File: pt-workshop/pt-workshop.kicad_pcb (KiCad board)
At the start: 2 copper layers, 53 parts, among them J101 Conn_01x10, J102 Conn_01x10, Q301 NST65011, Q401 J201, Q402 3904 BEC, U201 L78L05, U202 PT2399-Detailed, U301 TL972

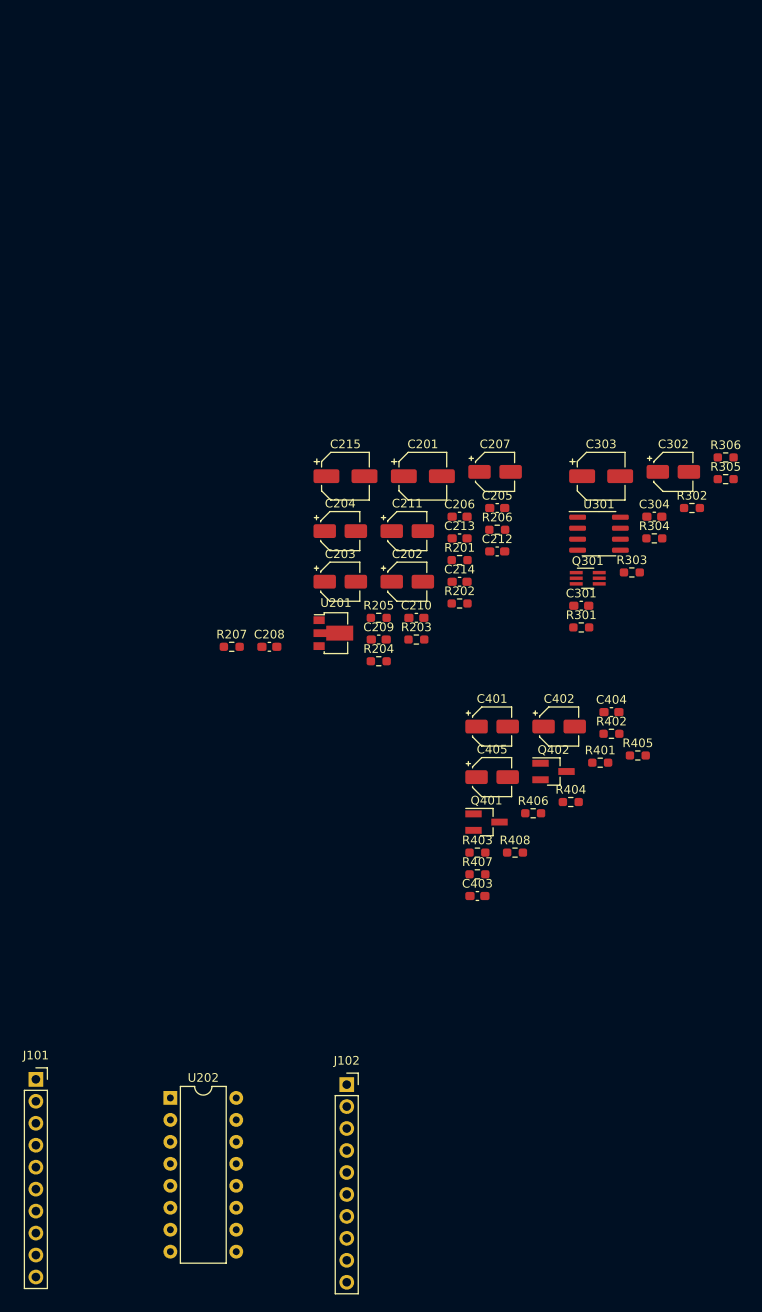
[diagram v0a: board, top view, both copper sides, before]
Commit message: 10 pin socket
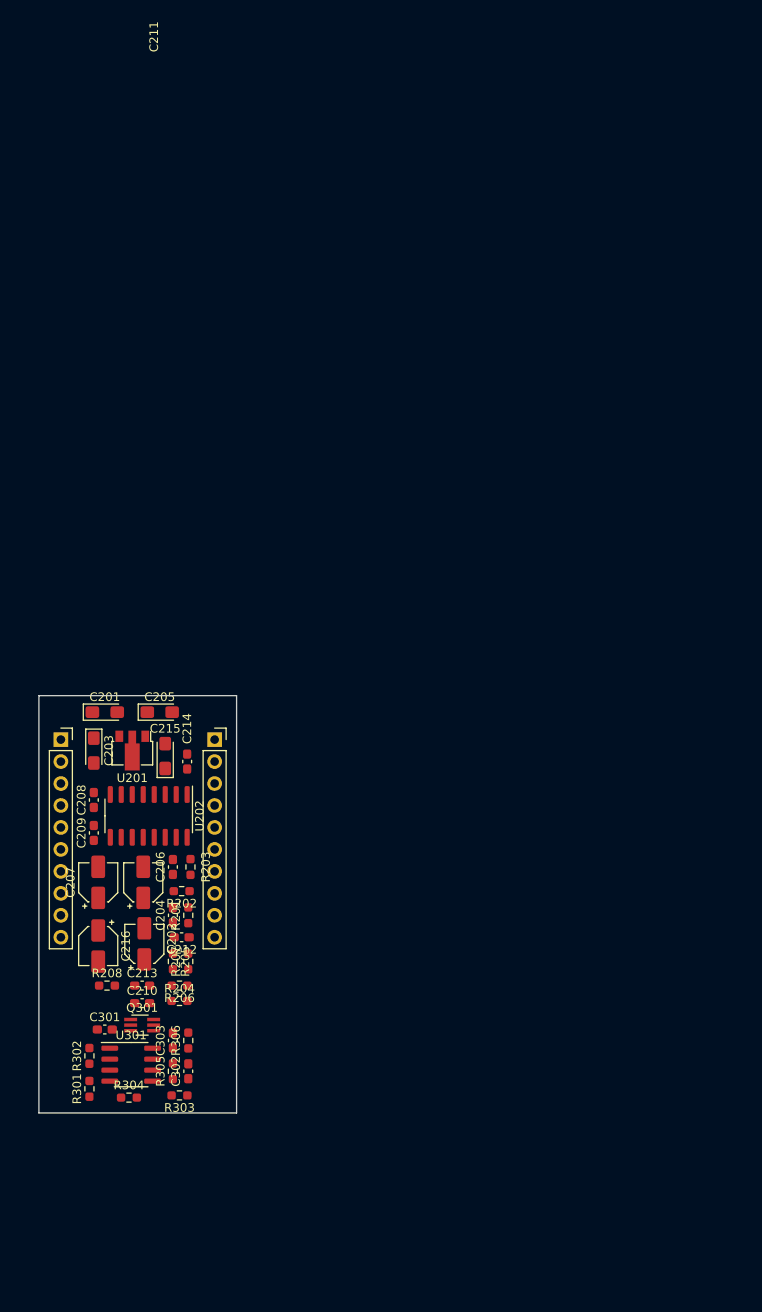
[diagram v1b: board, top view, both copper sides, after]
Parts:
- removed C304, C403, C404: 100n, Capacitor_SMD:C_0603_1608Metric_Pad1.08x0.95mm_HandSolder
- removed C401, C405: 4.7u, Capacitor_SMD:CP_Elec_4x5.4
- removed C402: 100n, Capacitor_SMD:CP_Elec_4x5.4
- removed Q401: J201, Package_TO_SOT_SMD:SOT-23_Handsoldering
- removed Q402: 3904 BEC, Package_TO_SOT_SMD:SOT-23_Handsoldering
- removed R401, R404: 1M, Resistor_SMD:R_0603_1608Metric_Pad0.98x0.95mm_HandSolder
- removed R402: 100K, Resistor_SMD:R_0603_1608Metric_Pad0.98x0.95mm_HandSolder
- removed R403, R406, R408: 10K, Resistor_SMD:R_0603_1608Metric_Pad0.98x0.95mm_HandSolder
- removed R405: 3.3K, Resistor_SMD:R_0603_1608Metric_Pad0.98x0.95mm_HandSolder
- removed R407: 1K, Resistor_SMD:R_0603_1608Metric_Pad0.98x0.95mm_HandSolder
- added C216: 4.7u, Capacitor_SMD:CP_Elec_4x5.4, F.Cu at (32.3, 84.8)
- added R208: 10K, Resistor_SMD:R_0603_1608Metric_Pad0.98x0.95mm_HandSolder, F.Cu at (33.3, 89.4)
- C201, C215: footprint Capacitor_SMD:CP_Elec_5x5.4 -> Capacitor_Tantalum_SMD:CP_EIA-3216-10_Kemet-I_Pad1.58x1.35mm_HandSolder
- C202: value 330n -> 4.7u
- C203: value 4.7u -> 330n; footprint Capacitor_SMD:CP_Elec_4x5.4 -> Capacitor_Tantalum_SMD:CP_EIA-3216-10_Kemet-I_Pad1.58x1.35mm_HandSolder
- C204: value 100n -> 3.9n; footprint Capacitor_SMD:CP_Elec_4x5.4 -> Capacitor_SMD:C_0603_1608Metric_Pad1.08x0.95mm_HandSolder
- C205: value 3.9n -> 100n; footprint Capacitor_SMD:C_0603_1608Metric_Pad1.08x0.95mm_HandSolder -> Capacitor_Tantalum_SMD:CP_EIA-3216-10_Kemet-I_Pad1.58x1.35mm_HandSolder
- C302: value 100n -> 10p; footprint Capacitor_SMD:CP_Elec_4x5.4 -> Capacitor_SMD:C_0603_1608Metric_Pad1.08x0.95mm_HandSolder
- C303: value 10u -> 100n; footprint Capacitor_SMD:CP_Elec_5x5.4 -> Capacitor_SMD:C_0603_1608Metric_Pad1.08x0.95mm_HandSolder
- R303, R304, R305: value 10K -> 100K
- R306: value 10 -> 10K
- U202: footprint Package_DIP:DIP-16_W7.62mm -> Package_SO:SOIC-16_3.9x9.9mm_P1.27mm
- moved R302 94.2 mm to (31.2, 97.5), turned to 90 degrees
- moved R305 93.7 mm to (40.9, 99.3), turned to 90 degrees
- moved R306 91.7 mm to (42.7, 95.8), turned to 90 degrees
- moved C302 89.2 mm to (42.7, 99.3), turned to 90 degrees
- moved R304 88.7 mm to (35.8, 102.4)
- moved C303 81.9 mm to (40.9, 95.8), turned to 90 degrees
- moved U301 81.8 mm to (36.1, 98.6)
- moved R303 80.0 mm to (41.7, 102.1), turned to 180 degrees
- moved R301 78.0 mm to (31.2, 101.3), turned to 90 degrees
- moved C301 73.7 mm to (33.0, 94.5)
- moved Q301 73.0 mm to (37.3, 94.0)
- moved C207 66.0 mm to (32.3, 77.5), turned to 90 degrees
- moved R206 64.3 mm to (41.7, 89.4), turned to 180 degrees
- moved C213 63.4 mm to (37.3, 89.4)
- moved C212 57.6 mm to (41.9, 83.8), turned to 180 degrees
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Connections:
- net /DelayOut renamed Net-(C213-Pad2)
- C202 pad 1: /PT_9V -> /PT_In
- C202 pad 2: /PT_GND -> Net-(C202-Pad2)
- C203 pad 1: /Buffers/Buf_Out -> /PT_9V
- C203 pad 2: Net-(C203-Pad2) -> /PT_GND
- C204 pad 1: /PT_5V -> /PT_GND
- C204 pad 2: /PT_GND -> Net-(C204-Pad2)
- C205 pad 1: /PT_GND -> /PT_5V
- C205 pad 2: Net-(C205-Pad2) -> /PT_GND
- C301 pad 1: Net-(C301-Pad1) -> Net-(U301-Pad2)
- C301 pad 2: Net-(C301-Pad2) -> Net-(U301-Pad1)
- C302 pad 2: /PT_GND -> Net-(C302-Pad2)
- C303 pad 1: /PT_4.5V -> /PT_9V
- J101 pad 10: /PT_9V -> /PT_AttVert3
- J101 pad 3: /PT_5V -> /PT_4.5V
- J101 pad 4: /PT_Ref -> /PT_5V
- J101 pad 8: /PT_GND -> /PT_4.5V
- J101 pad 9: /PT_GND -> /PT_AttVert2
- J102 pad 1: /PT_9V -> /PT_In
- J102 pad 10: /PT_9V -> /PT_Voffset
- J102 pad 3: /PT_In -> /PT_Out
- J102 pad 4: /PT_Out -> /PT_Ref
- J102 pad 8: /PT_Vin -> /PT_GND
- R201 pad 1: Net-(C203-Pad2) -> Net-(C202-Pad2)
- R201 pad 2: Net-(C205-Pad2) -> Net-(C204-Pad2)
- R202 pad 1: Net-(C205-Pad2) -> Net-(C204-Pad2)
- R203 pad 2: Net-(C205-Pad2) -> Net-(C204-Pad2)
- R301 pad 1: /PT_Vin -> /PT_AttVert3
- R301 pad 2: Net-(C301-Pad1) -> Net-(U301-Pad2)
- R302 pad 1: Net-(C301-Pad1) -> Net-(U301-Pad2)
- R302 pad 2: Net-(C301-Pad2) -> Net-(U301-Pad1)
- R303 pad 1: Net-(C301-Pad2) -> /PT_Voffset
- R303 pad 2: Net-(Q301-Pad2) -> Net-(C302-Pad1)
- R304 pad 1: Net-(C302-Pad1) -> Net-(U301-Pad1)
- R304 pad 2: /PT_9V -> Net-(C302-Pad1)
- R305 pad 1: /PT_GND -> Net-(C302-Pad1)
- R305 pad 2: Net-(C302-Pad1) -> Net-(C302-Pad2)
- R306 pad 1: Net-(R306-Pad1) -> Net-(C302-Pad2)
- R306 pad 2: /PT_4.5V -> Net-(Q301-Pad2)
- U301 pad 1: Net-(R306-Pad1) -> Net-(U301-Pad1)
- U301 pad 2: Net-(R306-Pad1) -> Net-(U301-Pad2)
- U301 pad 3: Net-(C302-Pad1) -> /PT_AttVert2
- U301 pad 6: Net-(C301-Pad1) -> Net-(C302-Pad1)
- U301 pad 7: Net-(C301-Pad2) -> Net-(C302-Pad2)
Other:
- board outline added: 22.9 x 48.3 mm

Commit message: Board layed out
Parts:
- removed J101, J102: Conn_01x10, Connector_PinSocket_2.54mm:PinSocket_1x10_P2.54mm_Vertical
- added J103: Conn_01x20, Connector_PinSocket_2.54mm:PinSocket_1x20_P2.54mm_Vertical, F.Cu at (27.9, 58.4)
- added J104: Conn_01x20, Connector_PinSocket_2.54mm:PinSocket_1x20_P2.54mm_Vertical, F.Cu at (45.7, 58.4)
- moved R304 2.47 mm to (35.8, 104.8)
- moved R301 2.27 mm to (30.7, 103.6)
- moved C204 1.91 mm to (42.8, 81.2)
- moved R201 1.66 mm to (41.0, 81.2)
- moved R302 1.54 mm to (30.7, 99.0)
- moved C302 1.45 mm to (42.7, 100.8)
- moved C303 1.45 mm to (40.9, 97.2)
- moved R305 1.45 mm to (40.9, 100.8)
- moved R306 1.45 mm to (42.7, 97.2)
- moved C301 1.45 mm to (33.0, 95.9)
- moved Q301 1.45 mm to (37.3, 95.4)
- moved R303 1.45 mm to (41.7, 103.6)
- moved U301 1.45 mm to (36.1, 100.0)
- moved C209 0.97 mm to (30.9, 71.4)
- moved C208 0.92 mm to (30.9, 67.7)
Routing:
- net /PT_4.5V: track 0.00 -> 87.8 mm
- net /PT_Ic: track 0.00 -> 48.1 mm
- net /PT_5V: track 0.00 -> 39.2 mm
- net /PT2399-adapter/DEMOD_OUT: track 0.00 -> 37.0 mm
- net /PT_Ref: track 0.00 -> 32.8 mm
- net /PT_In: track 0.00 -> 32.6 mm
- net /PT_Iout: track 0.00 -> 29.7 mm
- net /PT_Voffset: track 0.00 -> 29.4 mm
- net /PT_Out: track 0.00 -> 29.0 mm
- net /PT_CLK: track 0.00 -> 27.2 mm, vias 0 -> 1
- net Net-(C212-Pad1): track 0.00 -> 25.4 mm
- net /PT_AttVert3: track 0.00 -> 20.7 mm
- net Net-(C301-Pad1): track 0.00 -> 18.8 mm
- net /PT_AttVert2: track 0.00 -> 17.6 mm, vias 0 -> 1
- net Net-(C213-Pad2): track 0.00 -> 16.4 mm
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- added copper zone on B.Cu, net /PT_9V
- added copper zone on F.Cu, net /PT_9V
- added copper zone on In1.Cu, net /PT_GND
- added copper zone on In2.Cu, net /PT_GND
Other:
- board size 22.9 x 48.3 mm -> 22.9 x 53.3 mm
- copper layers 2 -> 4

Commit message: wip
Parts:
- moved C204 0.13 mm to (42.9, 81.2)

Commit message: wip
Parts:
- added H101: GND, MountingHole:MountingHole_3.2mm_M3_ISO14580_Pad, F.Cu at (43.2, 111.8)
- added H102: 1, MountingHole:MountingHole_3.2mm_M3, F.Cu at (30.5, 53.3)
- added H103: GND, MountingHole:MountingHole_3.2mm_M3_ISO14580_Pad, F.Cu at (30.5, 111.8)
- added H104: 2, MountingHole:MountingHole_3.2mm_M3, F.Cu at (43.2, 53.3)
- moved C210 4.06 mm to (33.3, 91.4)
- moved Q301 0.69 mm to (37.3, 94.7)
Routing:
- net Net-(C210-Pad2): track 6.37 -> 10.4 mm
- net /PT_GND: track 14.9 -> 16.1 mm
- net /PT_Iout: track 29.7 -> 28.7 mm
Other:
- board size 22.9 x 53.3 mm -> 22.9 x 68.6 mm

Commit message: wip
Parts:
- added kibuzzard-65AA5840: G***, kibuzzard-65AA5840, B.Cu at (41.9, 58.4)
- added kibuzzard-65AA5850: G***, kibuzzard-65AA5850, B.Cu at (41.9, 83.8)
- added kibuzzard-65AA5850: G***, kibuzzard-65AA5850, B.Cu at (41.9, 91.4)
- added kibuzzard-65AA5850: G***, kibuzzard-65AA5850, B.Cu at (41.9, 68.6)
- added kibuzzard-65AA5850: G***, kibuzzard-65AA5850, B.Cu at (41.9, 61.0)
- added kibuzzard-65AA5850: G***, kibuzzard-65AA5850, B.Cu at (41.9, 96.5)
- added kibuzzard-65AA5850: G***, kibuzzard-65AA5850, B.Cu at (41.9, 76.2)
- added kibuzzard-65AA5850: G***, kibuzzard-65AA5850, B.Cu at (41.9, 106.7)
- added kibuzzard-65AA5873: G***, kibuzzard-65AA5873, B.Cu at (41.9, 63.5)
- added kibuzzard-65AA58DD: G***, kibuzzard-65AA58DD, B.Cu at (41.9, 66.0)
- added kibuzzard-65AA58EE: G***, kibuzzard-65AA58EE, B.Cu at (41.9, 71.1)
- added kibuzzard-65AA5905: G***, kibuzzard-65AA5905, B.Cu at (41.9, 73.7)
- added kibuzzard-65AA592D: G***, kibuzzard-65AA592D, B.Cu at (41.9, 81.3)
- added kibuzzard-65AA59BE: G***, kibuzzard-65AA59BE, B.Cu at (41.9, 86.4)
- added kibuzzard-65AA59F3: G***, kibuzzard-65AA59F3, B.Cu at (41.9, 94.0)
- added kibuzzard-65AA5A57: G***, kibuzzard-65AA5A57, B.Cu at (41.9, 78.7)
- added kibuzzard-65AA5AB7: G***, kibuzzard-65AA5AB7, B.Cu at (41.9, 88.9)
- added kibuzzard-65AA5C27: G***, kibuzzard-65AA5C27, B.Cu at (41.9, 101.6)
- added kibuzzard-65AA5C3F: G***, kibuzzard-65AA5C3F, B.Cu at (41.9, 99.1)
- added kibuzzard-65AA5C71: G***, kibuzzard-65AA5C71, B.Cu at (41.3, 104.1)

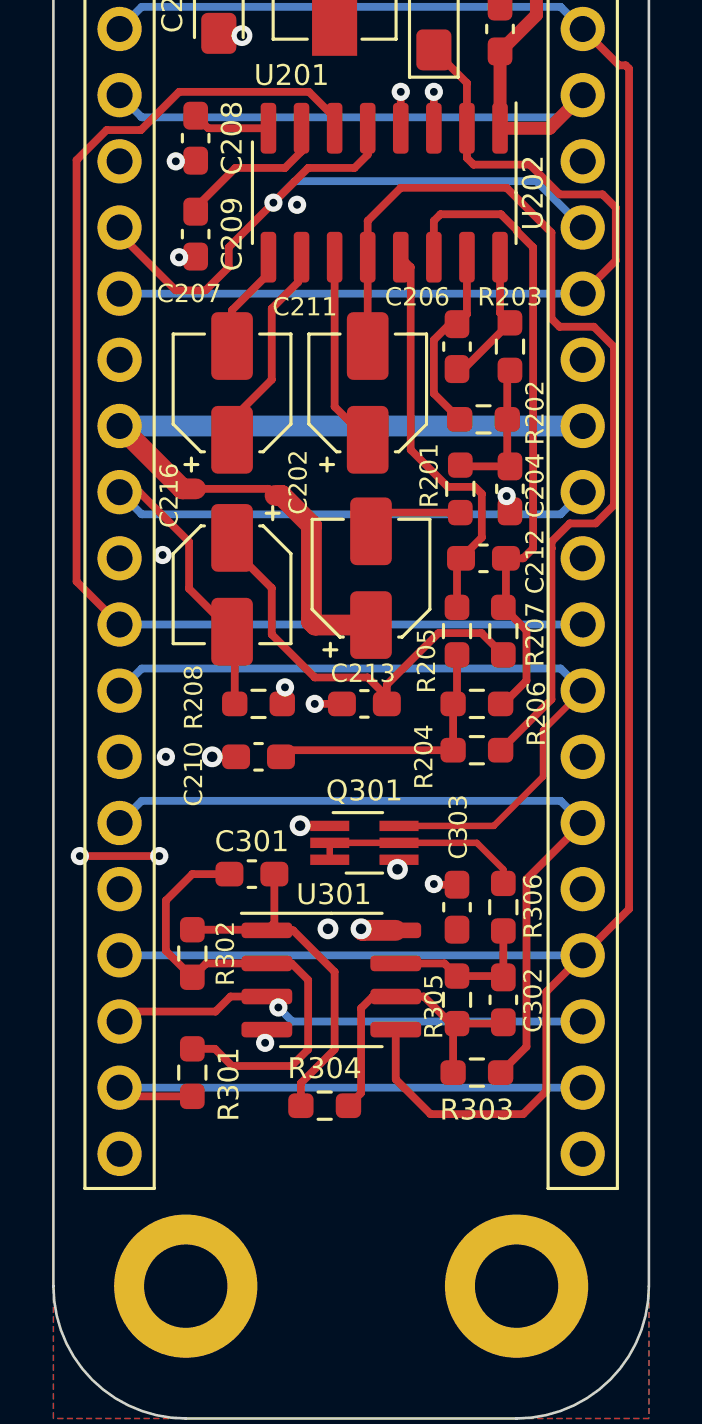
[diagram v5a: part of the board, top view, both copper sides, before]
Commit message: Mapped components
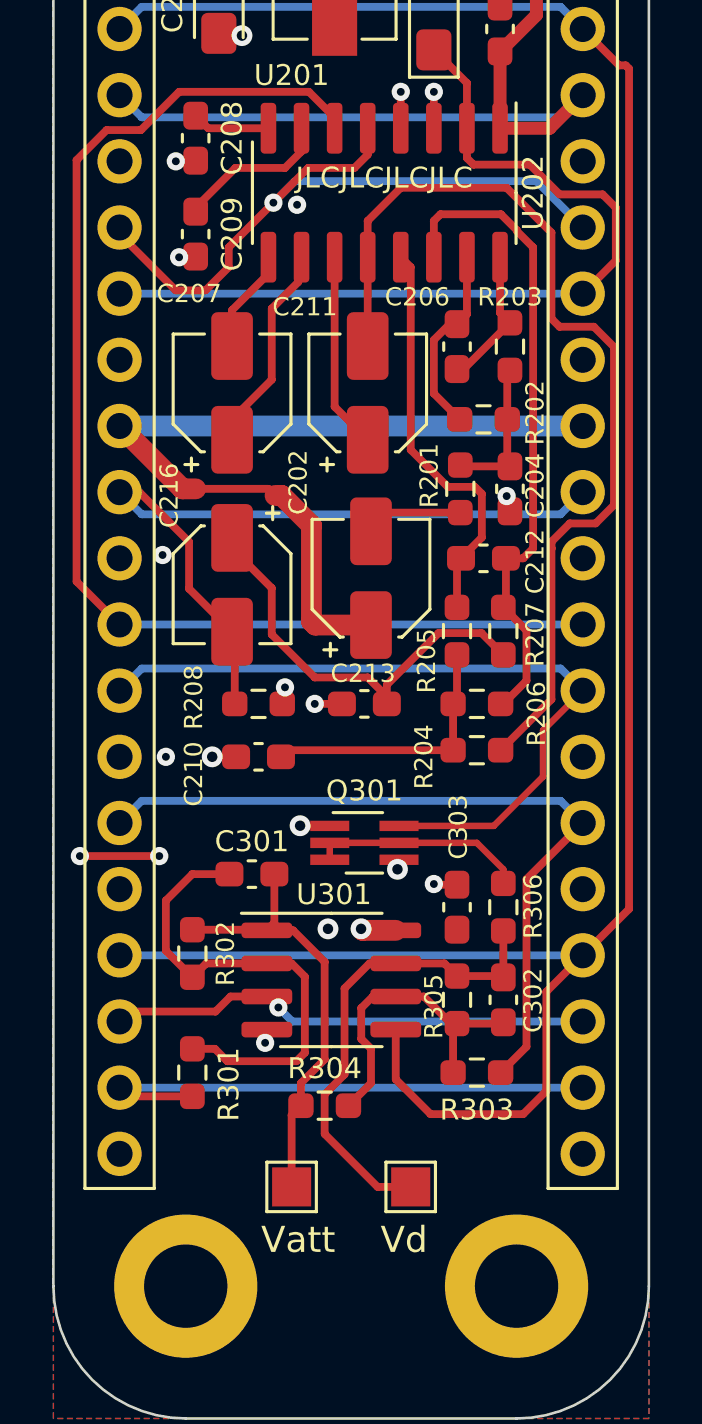
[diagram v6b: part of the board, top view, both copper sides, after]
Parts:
- added TP1: Vatt, TestPoint:TestPoint_Pad_1.5x1.5mm, F.Cu at (34.5, 108.0)
- added TP2: Vd, TestPoint:TestPoint_Pad_1.5x1.5mm, F.Cu at (39.1, 108.0)
- added kibuzzard-65AAA38B: G***, kibuzzard-65AAA38B, B.Cu at (31.8, 66.0)
- added kibuzzard-65AAA3AC: G***, kibuzzard-65AAA3AC, B.Cu at (31.8, 71.1)
- added kibuzzard-65AAA3BE: G***, kibuzzard-65AAA3BE, B.Cu at (31.8, 73.7)
- added kibuzzard-65AAA3D1: G***, kibuzzard-65AAA3D1, B.Cu at (31.8, 81.3)
- added kibuzzard-65AAA3DF: G***, kibuzzard-65AAA3DF, B.Cu at (31.8, 88.9)
- added kibuzzard-65AAA43F: G***, kibuzzard-65AAA43F, B.Cu at (31.8, 58.4)
- added kibuzzard-65AAA44C: G***, kibuzzard-65AAA44C, B.Cu at (31.8, 76.2)
- added kibuzzard-65AAA44C: G***, kibuzzard-65AAA44C, B.Cu at (31.8, 96.5)
- added kibuzzard-65AAA44C: G***, kibuzzard-65AAA44C, B.Cu at (31.8, 83.8)
- added kibuzzard-65AAA44C: G***, kibuzzard-65AAA44C, B.Cu at (31.8, 106.7)
- added kibuzzard-65AAA44C: G***, kibuzzard-65AAA44C, B.Cu at (31.8, 61.0)
- added kibuzzard-65AAA44C: G***, kibuzzard-65AAA44C, B.Cu at (31.8, 91.4)
- added kibuzzard-65AAA44C: G***, kibuzzard-65AAA44C, B.Cu at (31.8, 68.6)
- added kibuzzard-65AAA461: G***, kibuzzard-65AAA461, B.Cu at (31.8, 63.5)
- added kibuzzard-65AAA47E: G***, kibuzzard-65AAA47E, B.Cu at (31.8, 78.7)
- added kibuzzard-65AAA49E: G***, kibuzzard-65AAA49E, B.Cu at (31.8, 86.4)
- added kibuzzard-65AAA4B9: G***, kibuzzard-65AAA4B9, B.Cu at (31.8, 94.0)
- added kibuzzard-65AAA4E9: G***, kibuzzard-65AAA4E9, B.Cu at (31.8, 99.1)
- added kibuzzard-65AAA4EF: G***, kibuzzard-65AAA4EF, B.Cu at (31.8, 101.6)
- added kibuzzard-65AAA518: G***, kibuzzard-65AAA518, B.Cu at (32.4, 104.1)
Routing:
- net Net-(C302-Pad2): track 6.13 -> 18.5 mm
- net Net-(C301-Pad2): track 14.1 -> 17.0 mm
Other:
- board text added: "JLCJLCJLCJLC"

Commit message: v1rev1?
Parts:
- added G***: LOGO, LOGO, F.Cu at (36.8, 112.4)
- added REF**: OSHW-Logo2_7.3x6mm_SilkScreen, Symbol:OSHW-Logo2_7.3x6mm_SilkScreen, B.Cu at (36.8, 53.3)
- added kibuzzard-65ABC4A4: G***, kibuzzard-65ABC4A4, F.Cu at (36.8, 53.3)
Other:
- board text added: "PTT v1rev1"
- board text added: "pedalmarkt.com"

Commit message: wip
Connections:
- C202 pad 1: /PT_In -> Net-(C202-Pad1)
- C202 pad 2: Net-(C202-Pad2) -> /PT_In
- R201 pad 1: Net-(C202-Pad2) -> Net-(C202-Pad1)
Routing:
- net Net-(C202-Pad1): track 0.00 -> 5.74 mm
- net Net-(C202-Pad2): track 3.73 -> 0.00 mm
- net /PT_In: track 32.8 -> 29.1 mm
